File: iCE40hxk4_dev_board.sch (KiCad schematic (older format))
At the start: 0 parts

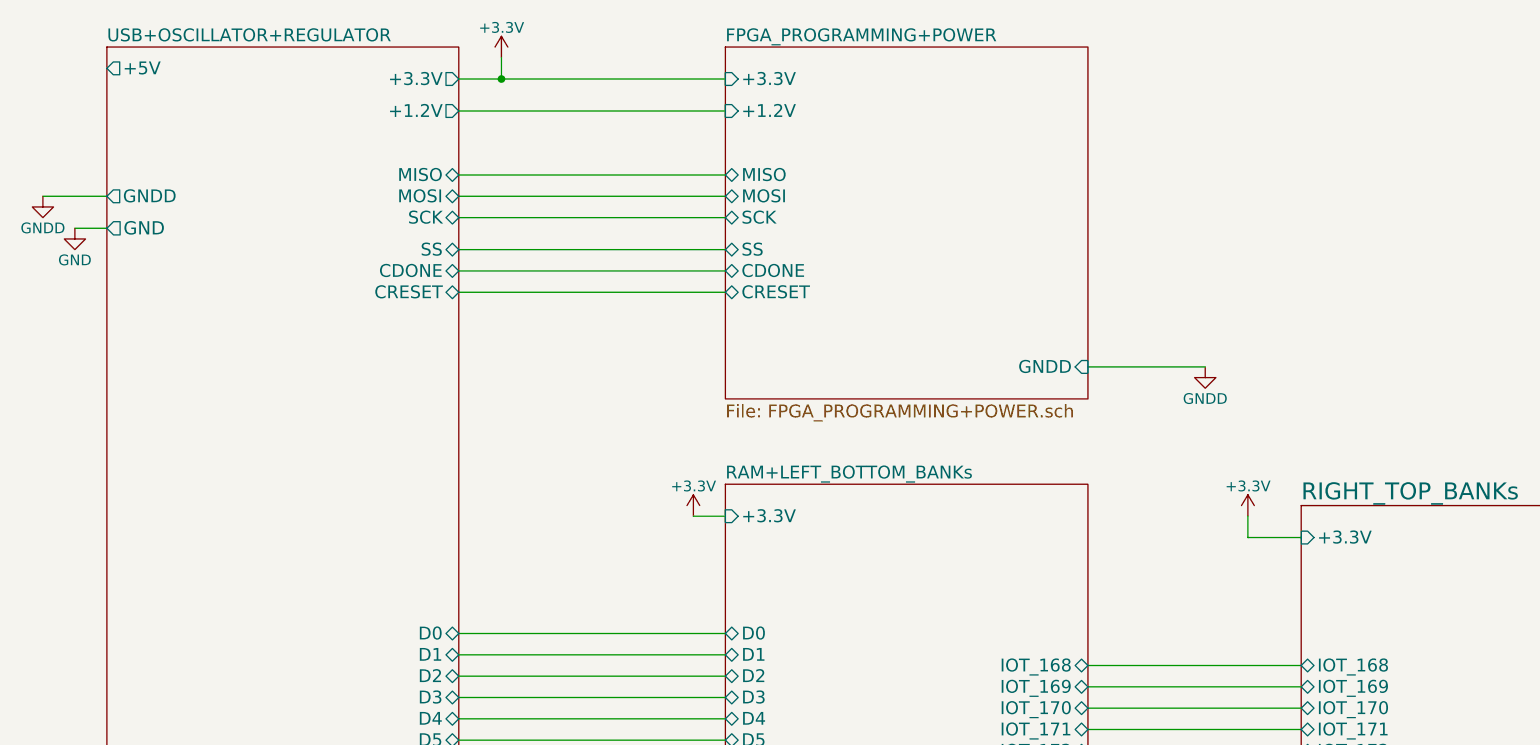
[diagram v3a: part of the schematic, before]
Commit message: Se conecta la tensión 5V a los conectores (right y left) y se cambia de nombre de un componente MIC2005A-2 -> MIC2005A-2YM5
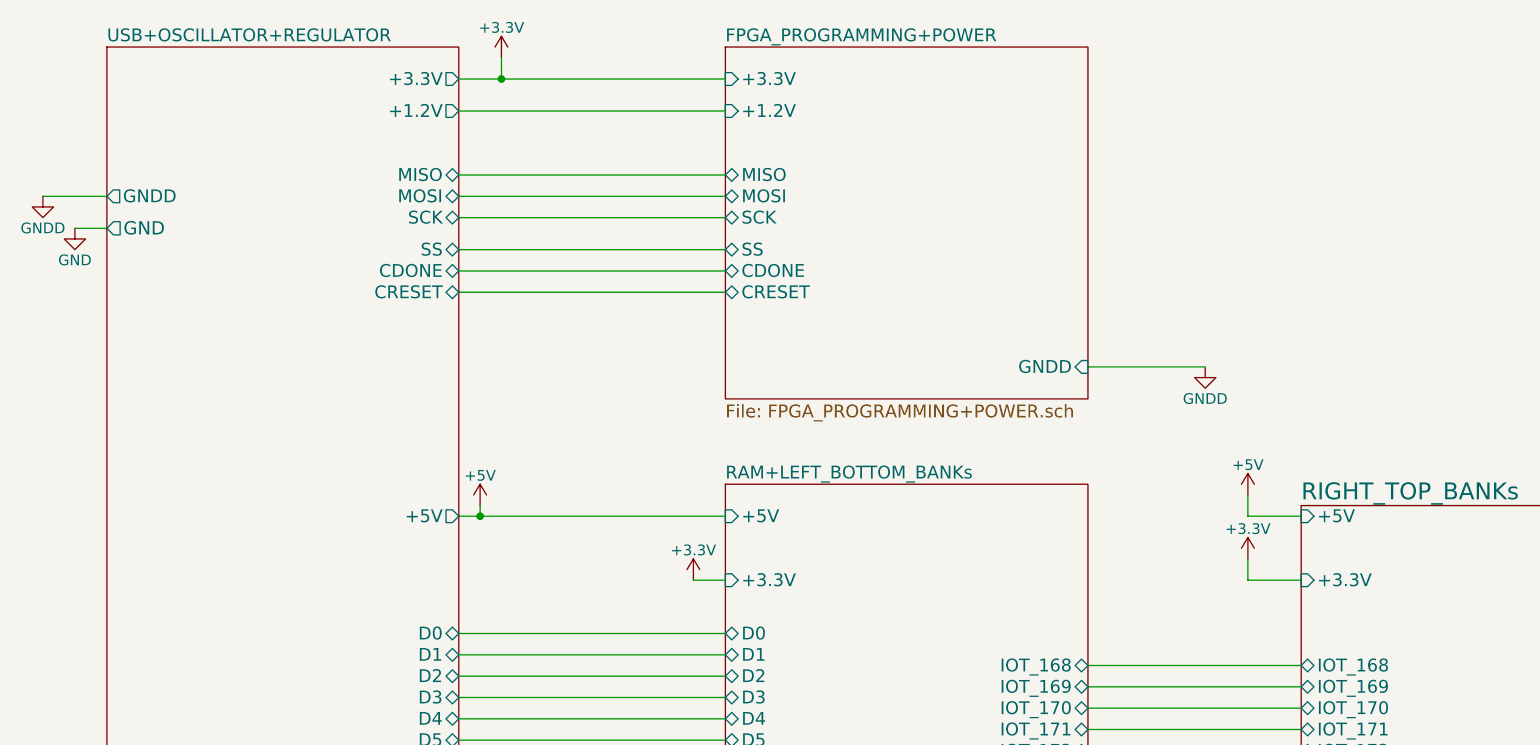
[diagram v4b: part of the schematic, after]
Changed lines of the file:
@@
 LIBS:MIC2005A-2
 LIBS:AS4C1M16S
-LIBS:iCE40hxk4_dev_board-cache
 EELAYER 25 0
 EELAYER END
@@
 F1 "USB+OSCILLATOR+REGULATOR.sch" 60
 F2 "+3.3V" O R 3900 1350 60
-F3 "+5V" O L 2250 1300 60
+F3 "+5V" O R 3900 3400 60
 F4 "+1.2V" O R 3900 1500 60
 F5 "GND" O L 2250 2050 62
@@
 L +3.3V #PWR03
 U 1 1 58DDF24C
-P 5000 3400
-F 0 "#PWR03" H 5000 3250 50  0001 C CNN
-F 1 "+3.3V" H 5000 3540 50  0000 C CNN
-F 2 "" H 5000 3400 50  0001 C CNN
-F 3 "" H 5000 3400 50  0001 C CNN
-	1    5000 3400
+P 5000 3700
+F 0 "#PWR03" H 5000 3550 50  0001 C CNN
+F 1 "+3.3V" H 5000 3840 50  0000 C CNN
+F 2 "" H 5000 3700 50  0001 C CNN
+F 3 "" H 5000 3700 50  0001 C CNN
+	1    5000 3700
 	1    0    0    -1
 $EndComp
@@
 Connection ~ 4100 1350
 Wire Wire Line
-	5150 3400 5000 3400
+	5150 3700 5000 3700
 Wire Wire Line
 	7200 5650 6850 5650
@@
 F27 "ADC_16" B R 9600 5350 60
 F28 "ADC_17" B R 9600 5450 60
-F29 "+3.3V" I L 7850 3500 60
+F29 "+3.3V" I L 7850 3700 60
 F30 "GNDD" I R 9600 5700 60
+F31 "+5V" I L 7850 3400 60
 $EndSheet
 Wire Wire Line
@@
 F0 "RAM+LEFT_BOTTOM_BANKs" 60
 F1 "RAM+LEFT_BOTTOM_BANKs.sch" 60
-F2 "+3.3V" I L 5150 3400 60
+F2 "+3.3V" I L 5150 3700 60
 F3 "GNDD" I R 6850 5650 60
 F4 "D0" B L 5150 3950 60
@@
 F24 "DQ15" B R 6850 5250 60
 F25 "DQ14" B R 6850 5150 60
+F26 "+5V" I L 5150 3400 60
 $EndSheet
 Wire Wire Line
@@
 L +3.3V #PWR09
 U 1 1 58F7EC7E
-P 7600 3400
-F 0 "#PWR09" H 7600 3250 50  0001 C CNN
-F 1 "+3.3V" H 7600 3540 50  0000 C CNN
-F 2 "" H 7600 3400 50  0001 C CNN
-F 3 "" H 7600 3400 50  0001 C CNN
-	1    7600 3400
-	1    0    0    -1
-$EndComp
-Wire Wire Line
-	7850 3500 7600 3500
-Wire Wire Line
-	7600 3500 7600 3400
+P 7600 3600
+F 0 "#PWR09" H 7600 3450 50  0001 C CNN
+F 1 "+3.3V" H 7600 3740 50  0000 C CNN
+F 2 "" H 7600 3600 50  0001 C CNN
+F 3 "" H 7600 3600 50  0001 C CNN
+	1    7600 3600
+	1    0    0    -1
+$EndComp
+Wire Wire Line
+	7850 3700 7600 3700
+Wire Wire Line
+	7600 3700 7600 3600
 $Comp
 L GNDD #PWR010
@@
 Wire Wire Line
 	9600 5700 9800 5700
+Wire Wire Line
+	3900 3400 5150 3400
+$Comp
+L +5V #PWR011
+U 1 1 592DDA96
+P 4000 3350
+F 0 "#PWR011" H 4000 3200 50  0001 C CNN
+F 1 "+5V" H 4000 3490 50  0000 C CNN
+F 2 "" H 4000 3350 50  0001 C CNN
+F 3 "" H 4000 3350 50  0001 C CNN
+	1    4000 3350
+	1    0    0    -1
+$EndComp
+$Comp
+L +5V #PWR012
+U 1 1 592DF050
+P 7600 3300
+F 0 "#PWR012" H 7600 3150 50  0001 C CNN
+F 1 "+5V" H 7600 3440 50  0000 C CNN
+F 2 "" H 7600 3300 50  0001 C CNN
+F 3 "" H 7600 3300 50  0001 C CNN
+	1    7600 3300
+	1    0    0    -1
+$EndComp
+Wire Wire Line
+	7600 3400 7850 3400
+Wire Wire Line
+	7600 3300 7600 3400
+Wire Wire Line
+	4000 3350 4000 3400
+Connection ~ 4000 3400
 $EndSCHEMATC

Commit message: Routing
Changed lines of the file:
@@
 Wire Wire Line
 	6850 4700 7850 4700
-$Sheet
-S 5150 3250 1700 2550
-U 58DE85E5
-F0 "RAM+LEFT_BOTTOM_BANKs" 60
-F1 "RAM+LEFT_BOTTOM_BANKs.sch" 60
-F2 "+3.3V" I L 5150 3700 60
-F3 "GNDD" I R 6850 5650 60
-F4 "D0" B L 5150 3950 60
-F5 "D1" B L 5150 4050 60
-F6 "D2" B L 5150 4150 60
-F7 "D3" B L 5150 4250 60
-F8 "D4" B L 5150 4350 60
-F9 "D5" B L 5150 4450 60
-F10 "D6" B L 5150 4550 60
-F11 "D7" B L 5150 4650 60
-F12 "~RXF" B L 5150 4800 60
-F13 "~TXE" B L 5150 4900 60
-F14 "~RD" B L 5150 5000 60
-F15 "~WR" B L 5150 5100 60
-F16 "SIWU" B L 5150 5200 60
-F17 "IOT_168" B R 6850 4100 60
-F18 "IOT_169" B R 6850 4200 60
-F19 "IOT_170" B R 6850 4300 60
-F20 "IOT_171" B R 6850 4400 60
-F21 "IOT_172" B R 6850 4500 60
-F22 "IOT_173" B R 6850 4600 60
-F23 "IOT_174" B R 6850 4700 60
-F24 "DQ15" B R 6850 5250 60
-F25 "DQ14" B R 6850 5150 60
-F26 "+5V" I L 5150 3400 60
-$EndSheet
 Wire Wire Line
 	6850 5250 7850 5250
@@
 	4000 3350 4000 3400
 Connection ~ 4000 3400
+$Sheet
+S 5150 3250 1700 2550
+U 58DE85E5
+F0 "RAM+LEFT_BOTTOM_BANKs" 60
+F1 "RAM+LEFT_BOTTOM_BANKs.sch" 60
+F2 "+3.3V" I L 5150 3700 60
+F3 "GNDD" I R 6850 5650 60
+F4 "D0" B L 5150 3950 60
+F5 "D1" B L 5150 4050 60
+F6 "D2" B L 5150 4150 60
+F7 "D3" B L 5150 4250 60
+F8 "D4" B L 5150 4350 60
+F9 "D5" B L 5150 4450 60
+F10 "D6" B L 5150 4550 60
+F11 "D7" B L 5150 4650 60
+F12 "~RXF" B L 5150 4800 60
+F13 "~TXE" B L 5150 4900 60
+F14 "~RD" B L 5150 5000 60
+F15 "~WR" B L 5150 5100 60
+F16 "SIWU" B L 5150 5200 60
+F17 "IOT_168" B R 6850 4100 60
+F18 "IOT_169" B R 6850 4200 60
+F19 "IOT_170" B R 6850 4300 60
+F20 "IOT_171" B R 6850 4400 60
+F21 "IOT_172" B R 6850 4500 60
+F22 "IOT_173" B R 6850 4600 60
+F23 "IOT_174" B R 6850 4700 60
+F24 "+5V" I L 5150 3400 60
+F25 "A4" I R 6850 5150 60
+F26 "A5" I R 6850 5250 60
+$EndSheet
 $EndSCHEMATC

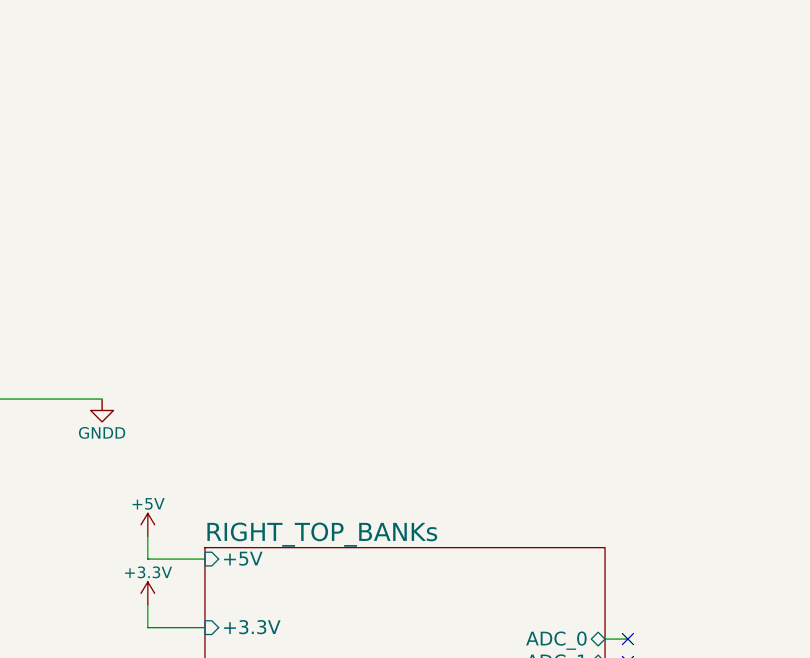
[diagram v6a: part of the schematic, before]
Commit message: Completed part selection of analog board. Merged analog and digital boards.
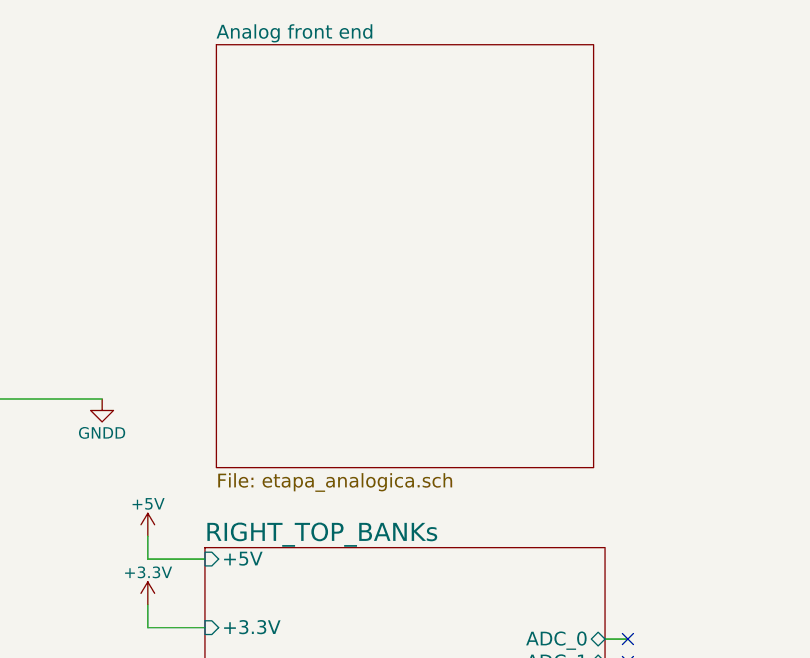
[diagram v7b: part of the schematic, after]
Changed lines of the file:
@@
 LIBS:MIC2005A-2
 LIBS:AS4C1M16S
+LIBS:adc1175
+LIBS:clc4007
+LIBS:DACs
+LIBS:d_schottky_300mv
+LIBS:lm337-n
+LIBS:lm4040dym3-2
+LIBS:max1720
+LIBS:MCP4716
+LIBS:mic7300
+LIBS:multiplexors
+LIBS:tcr2ef13
+LIBS:voltage-references
+LIBS:voltage-regulators
 LIBS:iCE40hxk4_dev_board-cache
 EELAYER 25 0
@@
 $Descr A4 11693 8268
 encoding utf-8
-Sheet 1 5
+Sheet 1 11
 Title ""
 Date ""
@@
 F26 "A5" I R 6850 5250 60
 $EndSheet
+$Sheet
+S 7900 1150 1650 1850
+U 594C84EF
+F0 "Analog front end" 60
+F1 "etapa_analogica.sch" 60
+$EndSheet
 $EndSCHEMATC

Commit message: ....
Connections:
- net labels added: GNDA
- wire segments 62 -> 64
